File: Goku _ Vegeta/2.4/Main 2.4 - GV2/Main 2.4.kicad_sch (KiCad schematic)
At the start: 40 parts, among them J1 JST-XH M1 ENC, J10 Conn_01x08_Female, J11 Motor Driver Inputs, J12 OpenMV H7, J13 JST-XH Screen, J14 Conn_01x08_Female, J15 Motor Driver 1 Power, J16 Motor Driver 2 Power, J17 Conn_01x08_Female, J18 Conn_01x18_Female, J19 Conn_01x10_Female, J2 JST-XH M2 ENC, J20 Conn_01x08_Female, J21 Conn_01x08_Female, J22 Conn_01x18_Female, J23 Line PCB 2, J24 B3B-XH-A(LF)(SN), J25 B2B-XH-A(LF)(SN), J3 JST-XH M3 ENC, J4 JST-XH M4 ENC, J5 XT60-M, J6 Voltmeter, J7 XT60-M, J8 XT60-M, J9 Line PCB 1, U1 DC-DC_Buck_Converter_7-24V_to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, U4 Adafruit_BNO055_STEMMA_QT

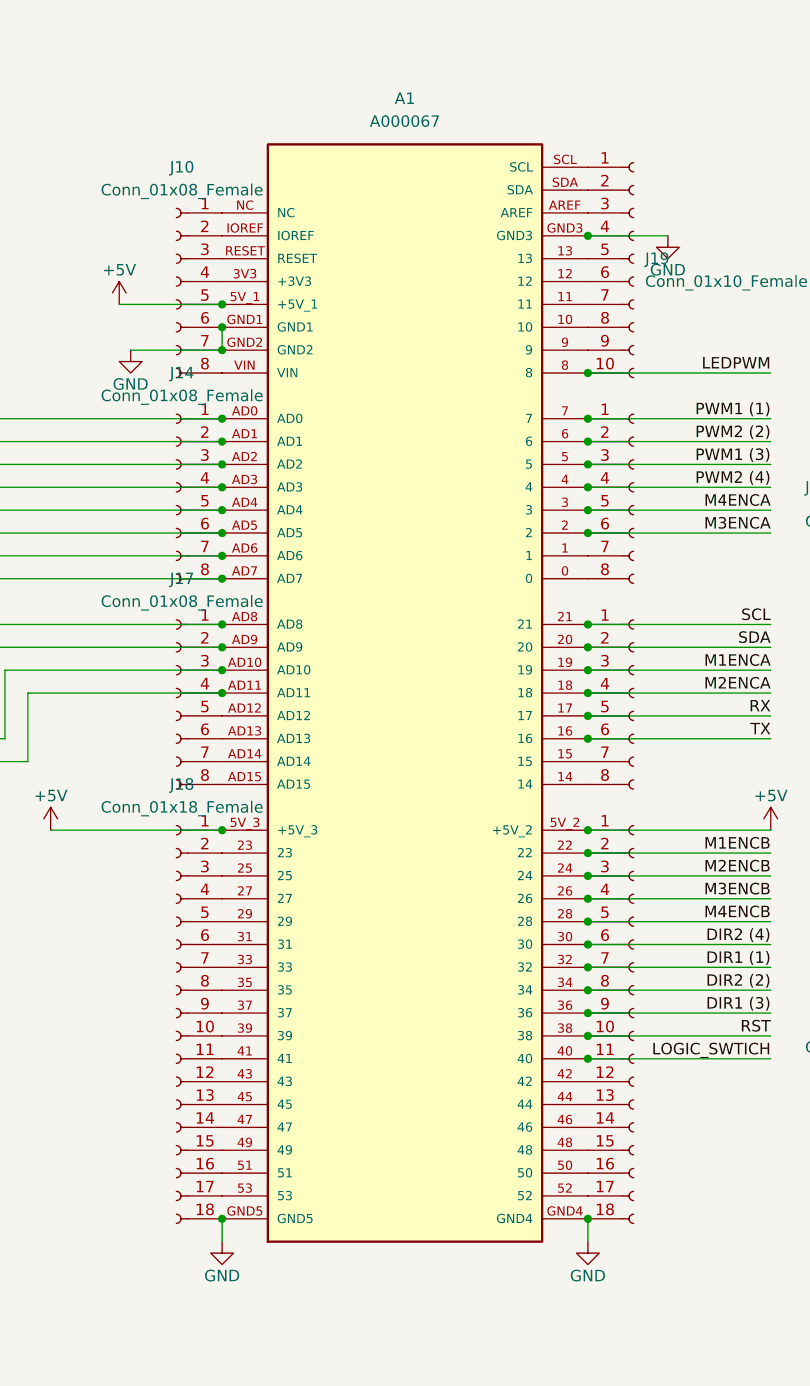
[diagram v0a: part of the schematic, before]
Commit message: Started 3.1 PCBs
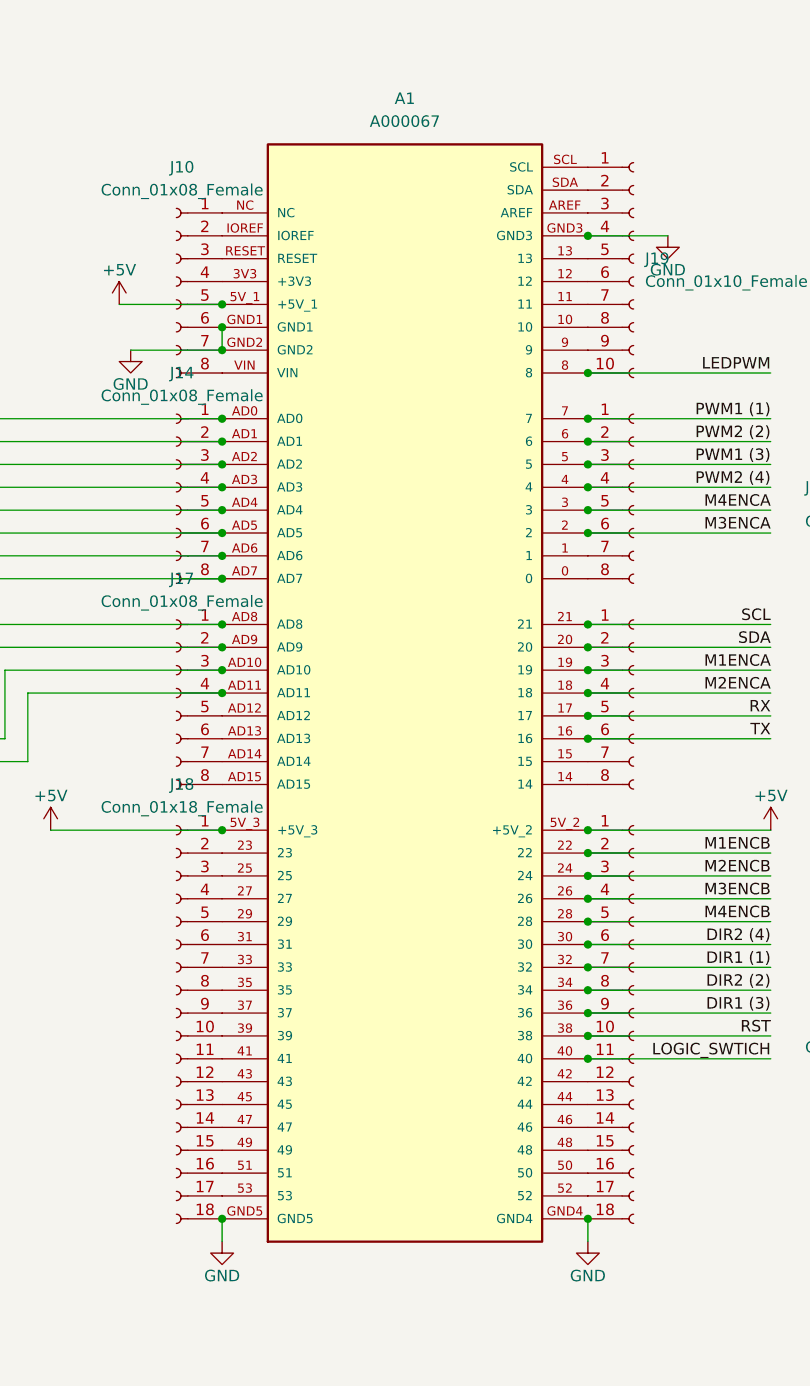
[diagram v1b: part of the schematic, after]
